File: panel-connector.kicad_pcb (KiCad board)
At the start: 2 copper layers, 95.9 x 90.2 mm, 200 parts, among them J1 PC104-8BIT, J105 MOLEX_FFC-14, J2 PC104PTH, J200 MOLEX_FFC-14, J201 CONN-TAB, J202 CONN-TAB, J203 CONN-TAB, J204 CONN-TAB, J210 MOLEX_FFC-14, J211 CONN-TAB, J212 CONN-TAB, J213 CONN-TAB, J214 CONN-TAB, J220 MOLEX_FFC-14, J221 CONN-TAB, J222 CONN-TAB, J223 CONN-TAB, J224 CONN-TAB, J230 MOLEX_FFC-14, J231 CONN-TAB, J232 CONN-TAB, J233 CONN-TAB, J234 CONN-TAB, J3 PC104PTH, J4 PC104PTH, J5 PC104PTH, U100 SPV1040, U110 SPV1040, U120 SPV1040, U130 SPV1040, U140 SPV1040, U150 SPV1040, U160 SPV1040, U170 SPV1040, U200 ADG728, U210 ADG728, U220 ADG728, U230 ADG728

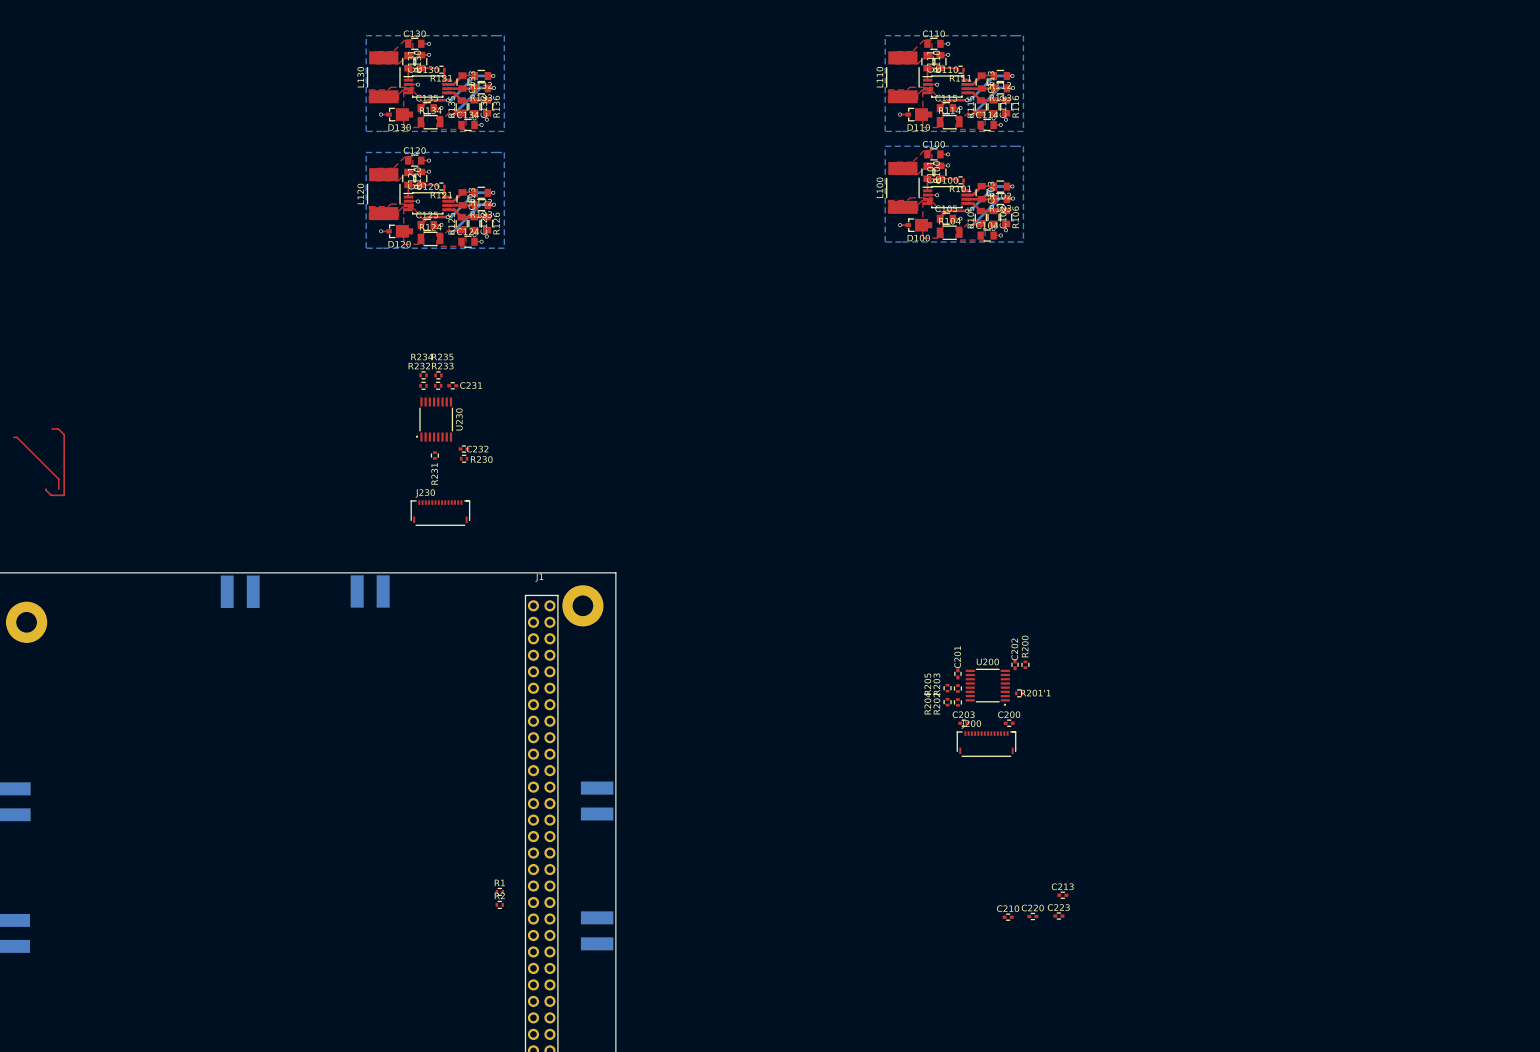
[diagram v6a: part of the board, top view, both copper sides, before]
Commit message: generated 3d model with gps
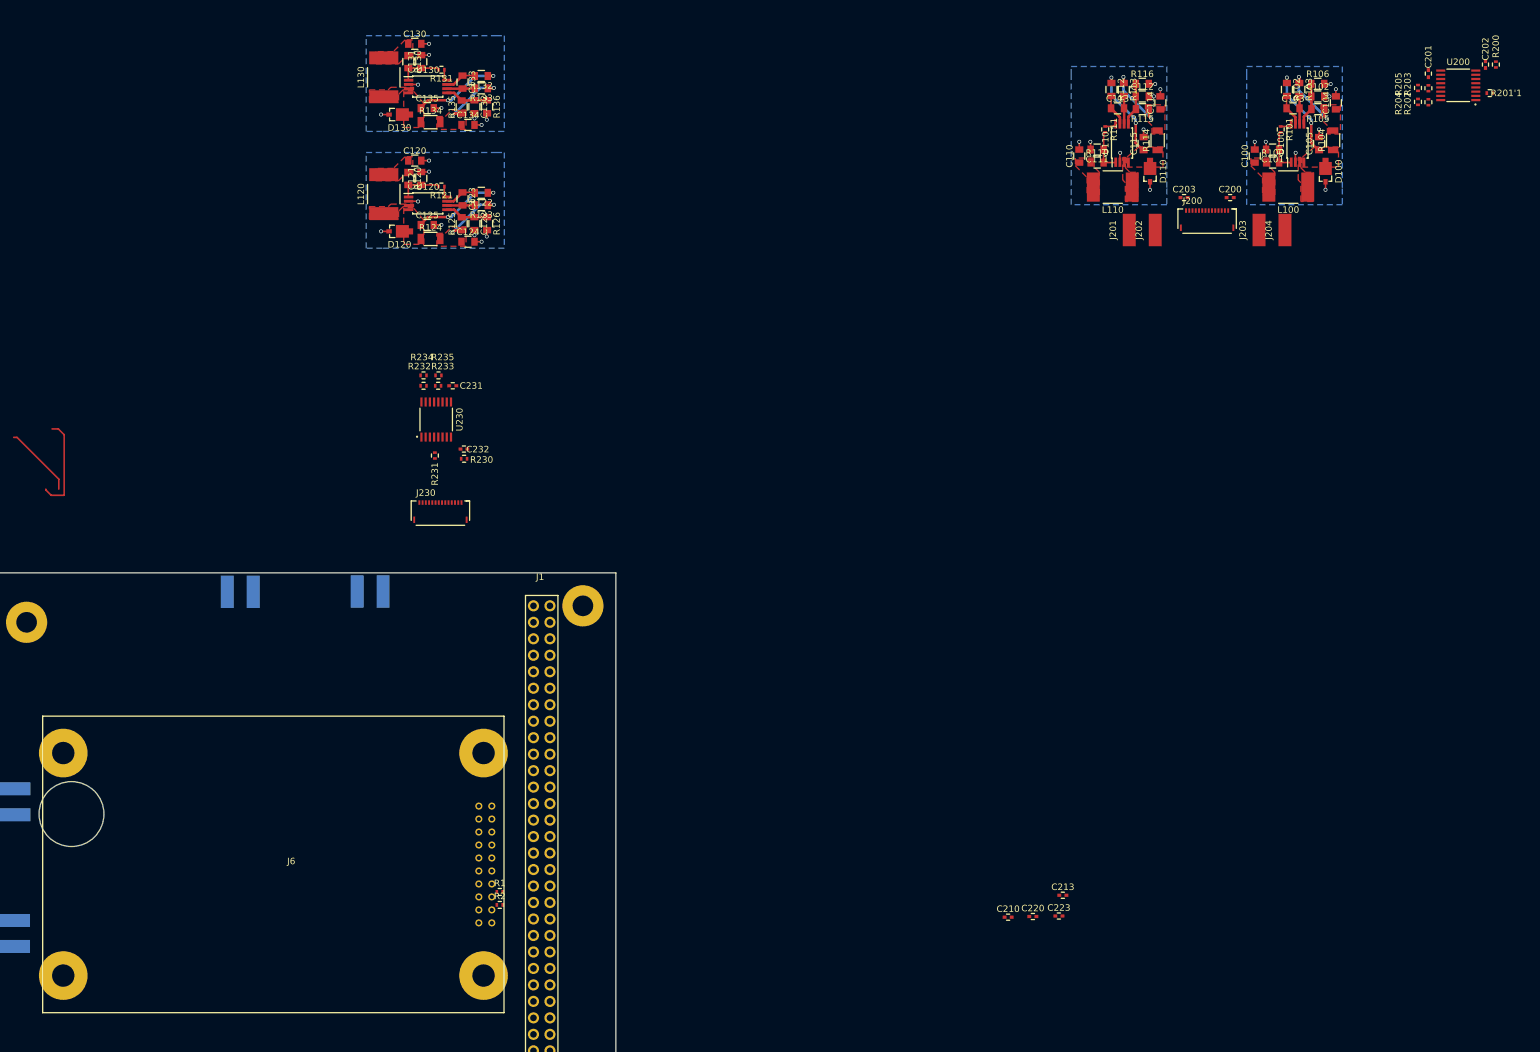
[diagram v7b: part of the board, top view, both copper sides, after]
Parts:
- added J6: OEM719, SFUSat:OEM719, F.Cu at (112.5, 112.6)
- J201, J202, J203, J204: moved to F.Cu
- moved J201 137.2 mm to (280.0, -8.00), turned to 270 degrees
- moved J202 136.5 mm to (284.0, -8.00), turned to 270 degrees
- moved J204 136.5 mm to (304.0, -8.00), turned to 270 degrees
- moved J203 136.0 mm to (300.0, -8.00), turned to 270 degrees
- moved C201 117.5 mm to (326.1, -32.1)
- moved R202 117.5 mm to (326.1, -27.7)
- moved R203 117.5 mm to (326.1, -29.9)
- moved C202 117.5 mm to (334.9, -33.5)
- moved R200 117.5 mm to (336.5, -33.5)
- moved R201'1 117.5 mm to (335.6, -29.1)
- moved R204 117.5 mm to (324.5, -27.8)
- moved R205 117.5 mm to (324.5, -29.9)
- moved U200 117.5 mm to (330.7, -30.3)
- moved C200 87.9 mm to (295.6, -13.0)
- moved C203 87.8 mm to (288.4, -13.0)
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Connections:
- J201 pad 1: /MPPT_X+_1/PV+ -> /MPPT_X+_2/PV+
- J202 pad 1: /MPPT_X+_1/PV- -> GND
- J203 pad 1: /MPPT_X+_2/PV+ -> /MPPT_X+_1/PV+
- J204 pad 1: GND -> /MPPT_X+_1/PV-
- J211 pad 1: /MPPT_X-_1/PV+ -> /MPPT_X-_2/PV+
- J212 pad 1: /MPPT_X-_1/PV- -> GND
- J213 pad 1: /MPPT_X-_2/PV+ -> /MPPT_X-_1/PV+
- J214 pad 1: GND -> /MPPT_X-_1/PV-
- J221 pad 1: /MPPT_Y+_1/PV+ -> /MPPT_Y+_2/PV+
- J222 pad 1: /MPPT_Y+_1/PV- -> GND
- J223 pad 1: /MPPT_Y+_2/PV+ -> /MPPT_Y+_1/PV+
- J224 pad 1: GND -> /MPPT_Y+_1/PV-
- J231 pad 1: /MPPT_Y-_2/PV+ -> /MPPT_Y-_1/PV+
- J232 pad 1: GND -> /MPPT_Y-_1/PV-
- J233 pad 1: /MPPT_Y-_1/PV+ -> /MPPT_Y-_2/PV+
- J234 pad 1: /MPPT_Y-_1/PV- -> GND
